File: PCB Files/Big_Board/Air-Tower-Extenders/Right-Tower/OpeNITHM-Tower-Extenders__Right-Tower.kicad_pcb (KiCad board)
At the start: 2 copper layers, 26.4 x 34.6 mm, 6 parts, among them J1 Conn_01x04_Male, J2 Conn_01x04_Male, J3 Conn_01x09_Male, J4 Conn_01x09_Male

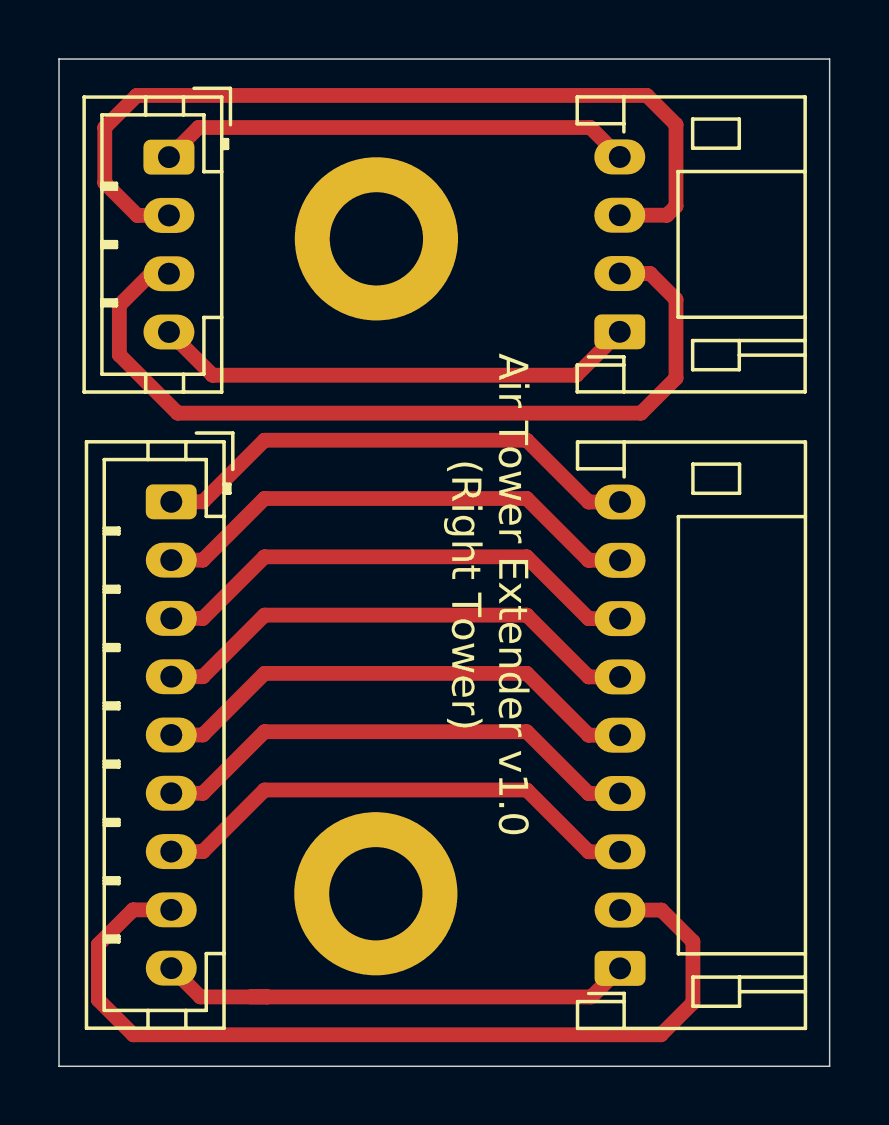
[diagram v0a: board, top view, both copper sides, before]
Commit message: Update the gerbers for the air extender PCBs
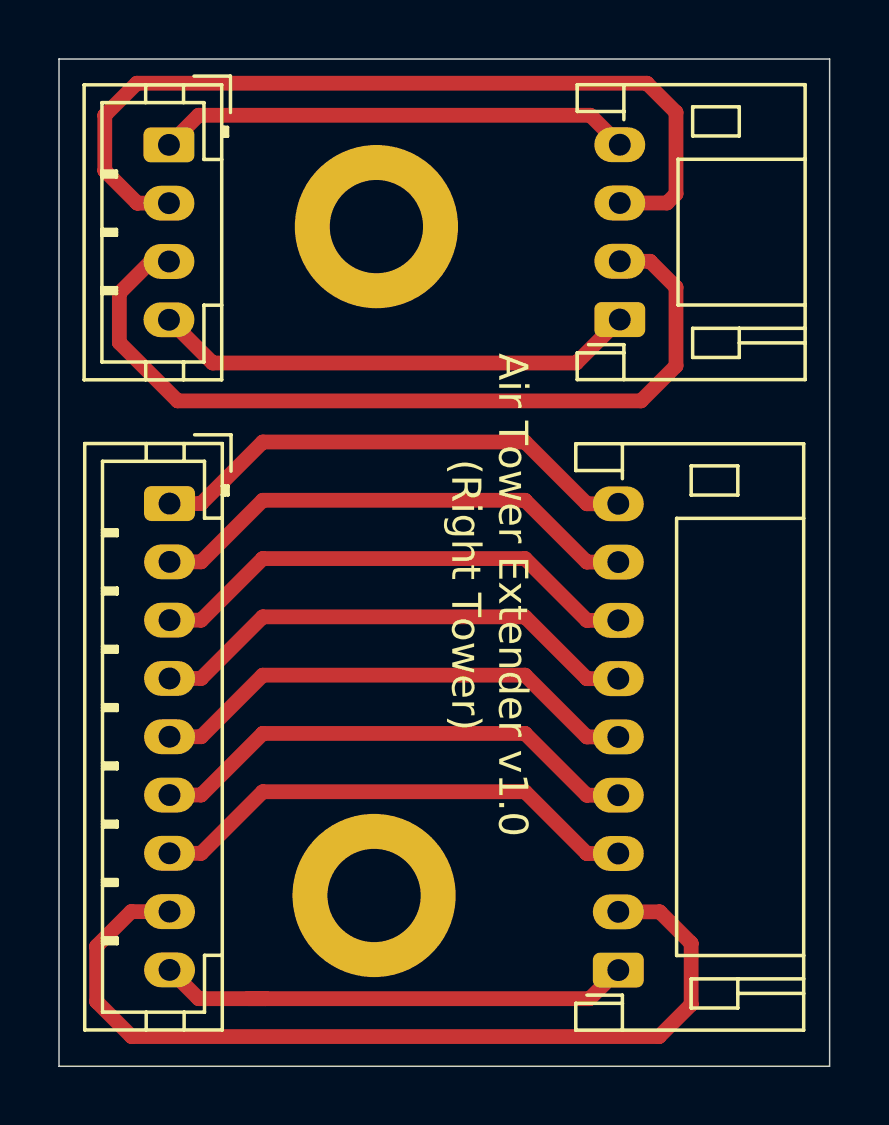
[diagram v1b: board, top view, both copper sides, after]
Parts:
- moved H1 0.42 mm to (73.8, 49.7)
- moved J1 0.42 mm to (66.7, 46.9)
- moved J2 0.42 mm to (82.2, 52.9)
- moved J3 0.08 mm to (66.7, 59.2)
- moved J4 0.08 mm to (82.1, 75.2)
- moved H2 0.08 mm to (73.8, 72.6)
